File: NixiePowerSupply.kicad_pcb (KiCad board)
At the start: 2 copper layers, 16 parts, among them J1 Conn_01x02, J2 Conn_01x02, Q1 IRF740, Q2 2N3905, U1 MC34063AP

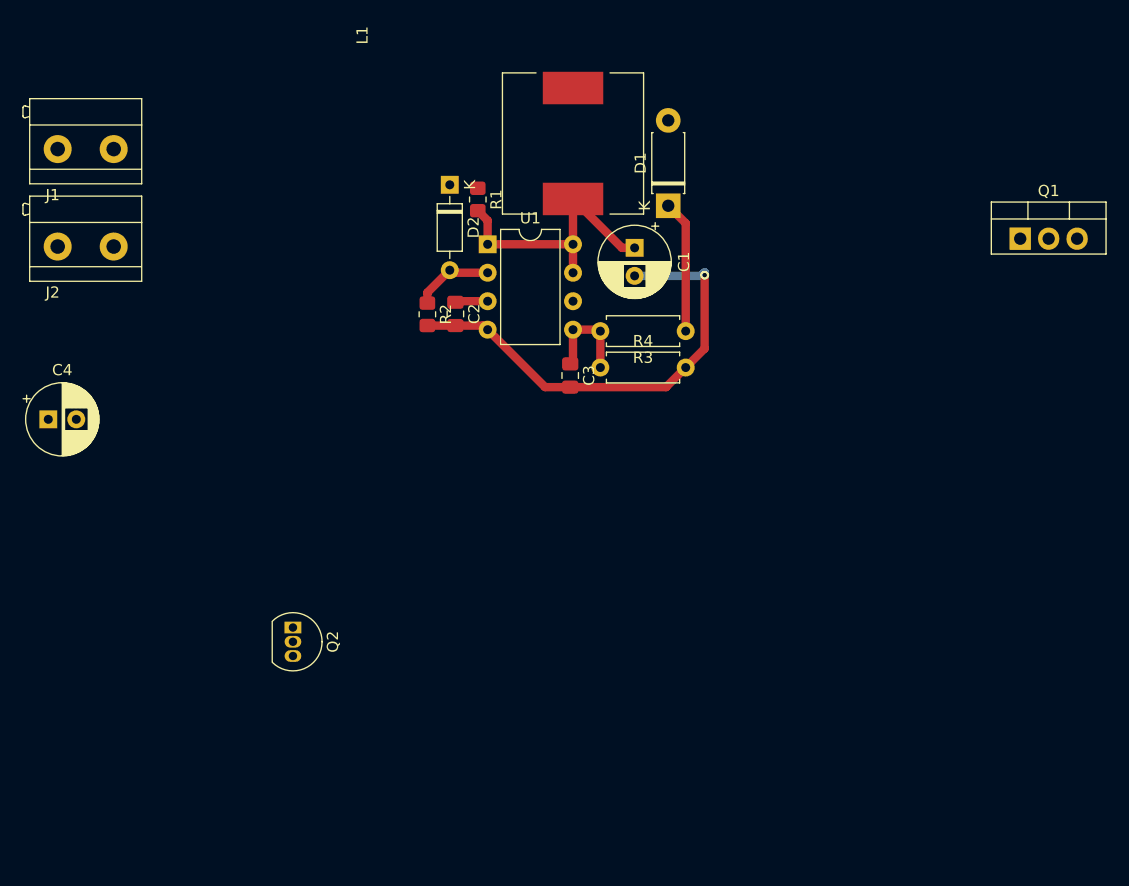
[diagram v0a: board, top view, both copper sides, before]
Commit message: first electrical circuit on pcb
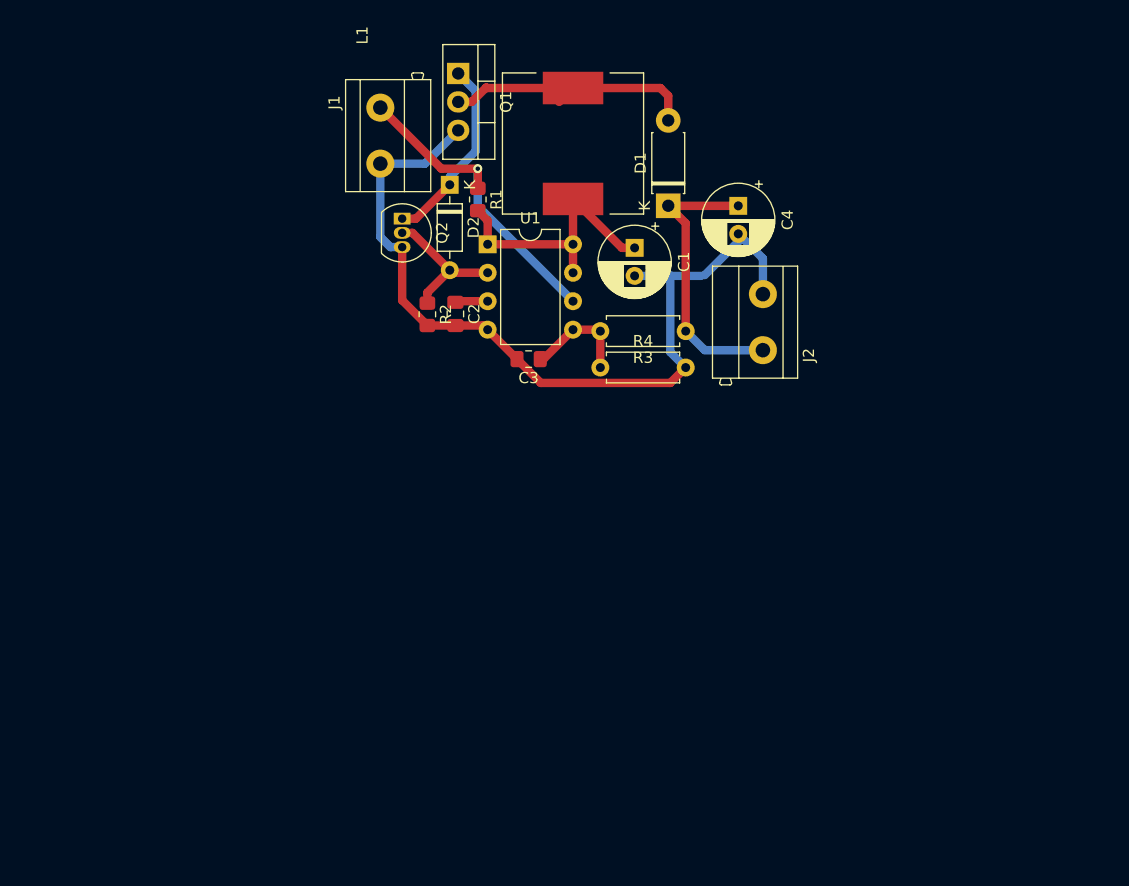
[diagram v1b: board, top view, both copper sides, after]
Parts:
- moved C4 64.5 mm to (146.8, 99.1), turned to -90 degrees
- moved J2 60.8 mm to (148.9, 109.5), turned to 90 degrees
- moved Q1 52.3 mm to (121.8, 87.2), turned to -90 degrees
- moved Q2 37.8 mm to (116.8, 100.2)
- moved J1 26.3 mm to (114.8, 92.8), turned to -90 degrees
- moved C3 3.99 mm to (128.0, 112.8), turned to 180 degrees
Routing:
- net GND: track 41.9 -> 76.7 mm, vias 1 -> 0
- net Net-(J1-Pin_1): track 0.00 -> 28.1 mm, vias 0 -> 1
- net Net-(D1-A): track 0.35 -> 23.9 mm
- net Net-(D2-K): track 0.00 -> 17.1 mm
- net Net-(D1-K): track 11.8 -> 25.7 mm
- net Net-(D2-A): track 7.24 -> 12.9 mm
- net Net-(U1-Vfb): track 8.90 -> 9.76 mm

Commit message: add outline
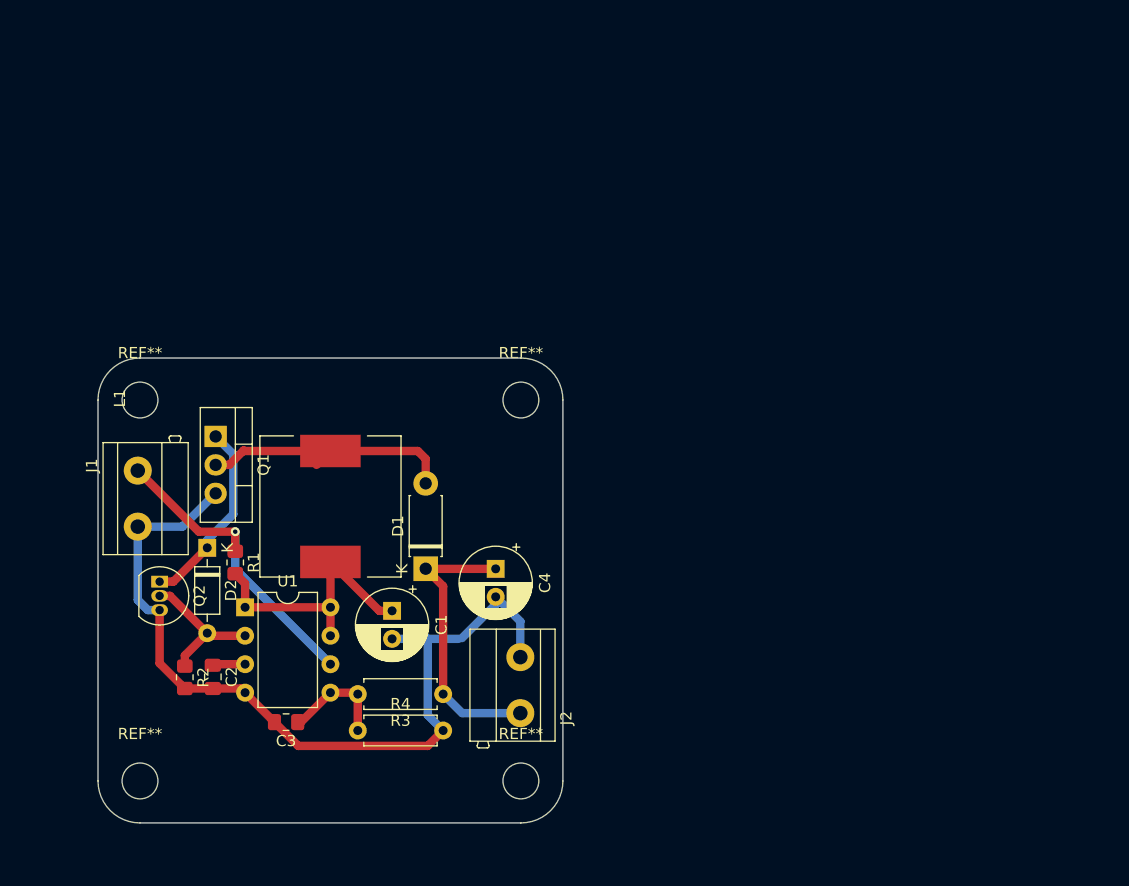
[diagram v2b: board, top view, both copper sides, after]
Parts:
- added REF**: MountingHole_3.2mm_M3, MountingHole:MountingHole_3.2mm_M3, F.Cu at (93.3, 116.4)
- added REF**: MountingHole_3.2mm_M3, MountingHole:MountingHole_3.2mm_M3, F.Cu at (127.3, 150.4)
- added REF**: MountingHole_3.2mm_M3, MountingHole:MountingHole_3.2mm_M3, F.Cu at (93.3, 150.4)
- added REF**: MountingHole_3.2mm_M3, MountingHole:MountingHole_3.2mm_M3, F.Cu at (127.3, 116.4)
- moved J1 39.0 mm to (93.1, 125.2)
- moved L1 39.0 mm to (110.3, 125.9)
- moved Q1 39.0 mm to (100.1, 119.7)
- moved Q2 39.0 mm to (95.1, 132.6)
- moved C1 39.0 mm to (115.8, 135.2)
- moved C2 39.0 mm to (99.8, 141.1)
- moved C4 39.0 mm to (125.1, 131.5)
- moved D1 39.0 mm to (118.8, 131.5)
- moved D2 39.0 mm to (99.3, 129.6)
- moved J2 39.0 mm to (127.3, 141.9)
- moved R1 39.0 mm to (101.8, 130.9)
- moved R2 39.0 mm to (97.3, 141.2)
- moved R3 39.0 mm to (120.4, 142.7)
- moved R4 39.0 mm to (112.8, 145.9)
- moved C3 39.0 mm to (106.4, 145.2)
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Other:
- board outline added: 41.5 x 41.5 mm

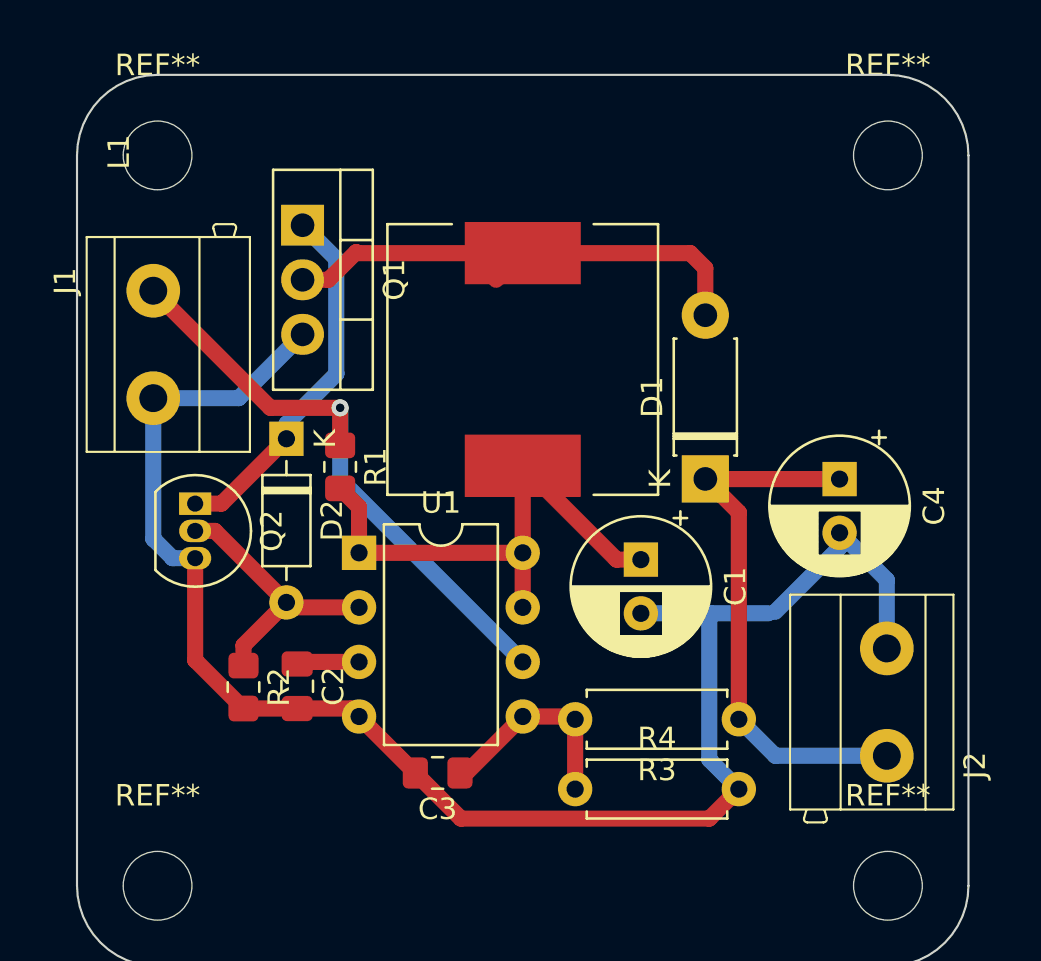
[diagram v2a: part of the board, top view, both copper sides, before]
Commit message: fix silk layer
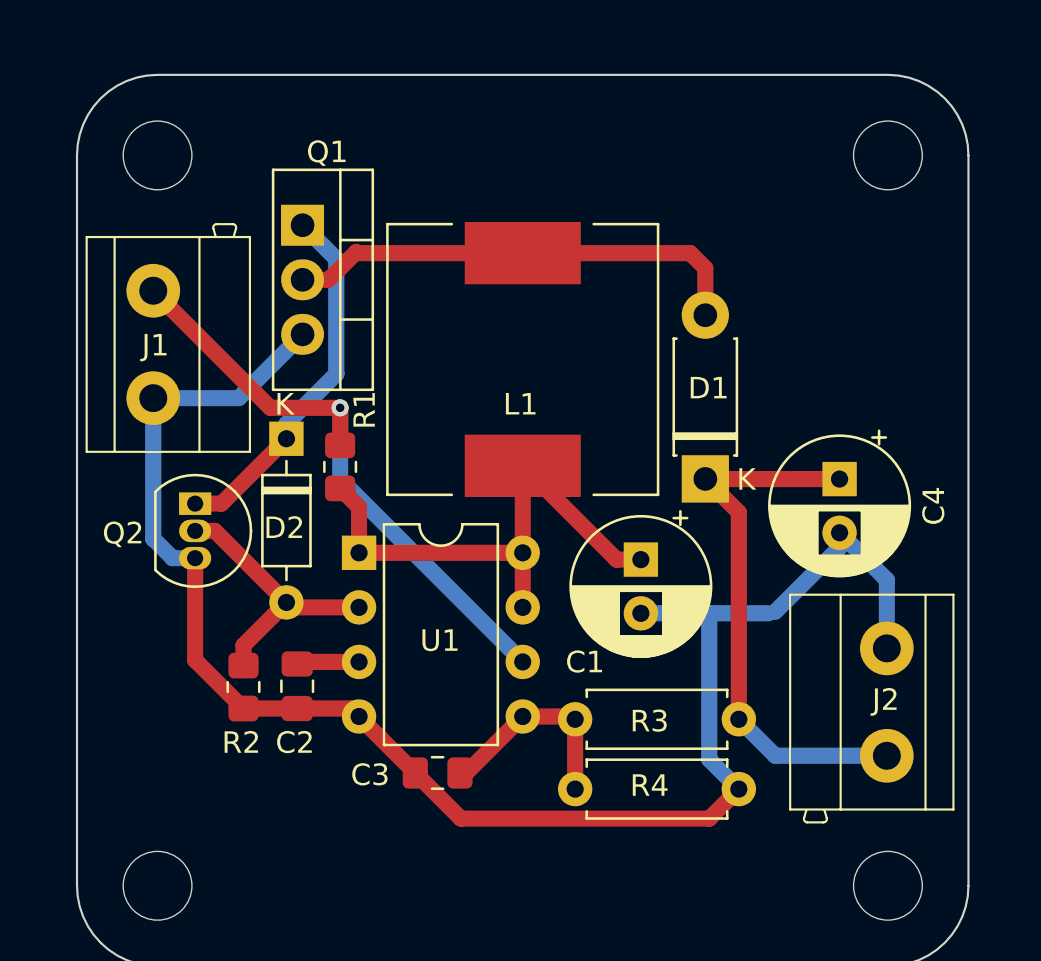
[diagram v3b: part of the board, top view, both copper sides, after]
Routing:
- net Net-(D1-A): track 23.9 -> 22.1 mm
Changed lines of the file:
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@@
     (property "ki_keywords" "connector")
     (attr through_hole)
-    (fp_text reference "J2" (at -2.95 4.1 90) (layer "F.SilkS")
+    (fp_text reference "J2" (at 0.10165 -0.04835) (layer "F.SilkS")
         (effects (font (size 1 1) (thickness 0.15)))
     )
@@
     (property "ki_keywords" "cap capacitor")
     (attr smd)
-    (fp_text reference "C2" (at 0 -1.68 90) (layer "F.SilkS")
+    (fp_text reference "C2" (at 2.63585 0.09835 -180) (layer "F.SilkS")
         (effects (font (size 1 1) (thickness 0.15)))
     )
@@
     (property "ki_keywords" "R res resistor")
     (attr through_hole)
-    (fp_text reference "R4" (at 3.81 -2.37) (layer "F.SilkS")
+    (fp_text reference "R4" (at 3.46165 -0.15165) (layer "F.SilkS")
         (effects (font (size 1 1) (thickness 0.15)))
     )
@@
     (tags "mounting hole 3.2mm no annular m3")
     (attr exclude_from_pos_files exclude_from_bom)
-    (fp_text reference "REF**" (at 0 -4.2) (layer "F.SilkS")
+    (fp_text reference "REF**" (at 0 -4.2) (layer "F.SilkS") hide
         (effects (font (size 1 1) (thickness 0.15)))
     )
@@
     (property "ki_keywords" "diode")
     (attr through_hole)
-    (fp_text reference "D1" (at 3.81 -2.47 90) (layer "F.SilkS")
+    (fp_text reference "D1" (at 4.21165 0.15165 180) (layer "F.SilkS")
         (effects (font (size 1 1) (thickness 0.15)))
     )
@@
         (effects (font (size 1 1) (thickness 0.15)))
     )
-    (fp_text user "K" (at 0 -2.1 90) (layer "F.SilkS")
+    (fp_text user "K" (at -0.03835 1.90165 180) (layer "F.SilkS")
         (effects (font (size 1 1) (thickness 0.15)))
     )
@@
     (property "ki_keywords" "diode")
     (attr through_hole)
-    (fp_text reference "D2" (at 3.81 -2.12 90) (layer "F.SilkS")
+    (fp_text reference "D2" (at 4.15835 0.09835 -180) (layer "F.SilkS")
         (effects (font (size 1 1) (thickness 0.15)))
     )
@@
         (effects (font (size 1 1) (thickness 0.15)))
     )
-    (fp_text user "K" (at 0 -1.8 90) (layer "F.SilkS")
+    (fp_text user "K" (at -1.59165 0.09835 -180) (layer "F.SilkS")
         (effects (font (size 1 1) (thickness 0.15)))
     )
@@
     (property "ki_keywords" "R res resistor")
     (attr smd)
-    (fp_text reference "R1" (at 0 -1.65 90) (layer "F.SilkS")
+    (fp_text reference "R1" (at -2.65165 -1.15165 90) (layer "F.SilkS")
         (effects (font (size 1 1) (thickness 0.15)))
     )
@@
     (property "ki_keywords" "R res resistor")
     (attr smd)
-    (fp_text reference "R2" (at 0 -1.65 90) (layer "F.SilkS")
+    (fp_text reference "R2" (at 2.59835 0.09835 -180) (layer "F.SilkS")
         (effects (font (size 1 1) (thickness 0.15)))
     )
@@
     (property "ki_keywords" "inductor choke coil reactor magnetic")
     (attr smd)
-    (fp_text reference "L1" (at 9.6575 -18.8 90) (layer "F.SilkS")
+    (fp_text reference "L1" (at -2.09835 -0.09835 180) (layer "F.SilkS")
         (effects (font (size 1 1) (thickness 0.15)))
     )
@@
     (tags "mounting hole 3.2mm no annular m3")
     (attr exclude_from_pos_files exclude_from_bom)
-    (fp_text reference "REF**" (at 0 -4.2) (layer "F.SilkS")
+    (fp_text reference "REF**" (at 0 -4.2) (layer "F.SilkS") hide
         (effects (font (size 1 1) (thickness 0.15)))
     )
@@
     (property "ki_keywords" "N Channel")
     (attr through_hole)
-    (fp_text reference "Q1" (at 2.54 -4.27 90) (layer "F.SilkS")
+    (fp_text reference "Q1" (at -3.40165 -1.15165 -180) (layer "F.SilkS")
         (effects (font (size 1 1) (thickness 0.15)))
     )
@@
     (property "ki_keywords" "cap capacitor")
     (attr through_hole)
-    (fp_text reference "C1" (at 1.25 -4.4 90) (layer "F.SilkS")
+    (fp_text reference "C1" (at 4.78073 2.59835 -180) (layer "F.SilkS")
         (effects (font (size 1 1) (thickness 0.15)))
     )
@@
     (property "ki_keywords" "smps buck boost inverting")
     (attr through_hole)
-    (fp_text reference "U1" (at 3.81 -2.33) (layer "F.SilkS")
+    (fp_text reference "U1" (at 3.77165 4.09835) (layer "F.SilkS")
         (effects (font (size 1 1) (thickness 0.15)))
     )
@@
     (tags "mounting hole 3.2mm no annular m3")
     (attr exclude_from_pos_files exclude_from_bom)
-    (fp_text reference "REF**" (at 0 -4.2) (layer "F.SilkS")
+    (fp_text reference "REF**" (at 0 -4.2) (layer "F.SilkS") hide
         (effects (font (size 1 1) (thickness 0.15)))
     )
@@
     (property "ki_keywords" "connector")
     (attr through_hole)
-    (fp_text reference "J1" (at -2.95 4.1 90) (layer "F.SilkS")
+    (fp_text reference "J1" (at 0.04835 -0.10165) (layer "F.SilkS")
         (effects (font (size 1 1) (thickness 0.15)))
     )
@@
     (property "ki_keywords" "R res resistor")
     (attr through_hole)
-    (fp_text reference "R3" (at 3.81 -2.37) (layer "F.SilkS")
+    (fp_text reference "R3" (at 4.15835 -0.09835) (layer "F.SilkS")
         (effects (font (size 1 1) (thickness 0.15)))
     )
@@
     (property "ki_keywords" "PNP Transistor")
     (attr through_hole)
-    (fp_text reference "Q2" (at 1.27 -3.56 90) (layer "F.SilkS")
+    (fp_text reference "Q2" (at 1.38835 3.34835 -180) (layer "F.SilkS")
         (effects (font (size 1 1) (thickness 0.15)))
     )
@@
     (property "ki_keywords" "cap capacitor")
     (attr smd)
-    (fp_text reference "C3" (at 0 -1.68) (layer "F.SilkS")
+    (fp_text reference "C3" (at 3.13585 -0.09835) (layer "F.SilkS")
         (effects (font (size 1 1) (thickness 0.15)))
     )
@@
     (tags "mounting hole 3.2mm no annular m3")
     (attr exclude_from_pos_files exclude_from_bom)
-    (fp_text reference "REF**" (at 0 -4.2) (layer "F.SilkS")
+    (fp_text reference "REF**" (at 0 -4.2) (layer "F.SilkS") hide
         (effects (font (size 1 1) (thickness 0.15)))
     )
@@
   (segment (start 118.14835 120.95165) (end 110.34835 120.95165) (width 0.75) (layer "F.Cu") (net 6))
   (segment (start 102.64835 120.95165) (end 110.34835 120.95165) (width 0.75) (layer "F.Cu") (net 6))
-  (segment (start 109.10835 122.19165) (end 110.34835 120.95165) (width 0.75) (layer "F.Cu") (net 6))
   (segment (start 100.09835 122.19165) (end 101.30835 122.19165) (width 0.75) (layer "F.Cu") (net 6))
   (segment (start 95.09835 132.61165) (end 96.32835 132.61165) (width 0.75) (layer "F.Cu") (net 7))
